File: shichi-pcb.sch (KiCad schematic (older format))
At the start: 27 parts, among them J1 USB_C_Receptacle_HRO_TYPE-C-3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, J2 Conn_01x04_Male, J3 Conn_01x06_Male, J4 Conn_01x04_Male, J5 Conn_01x01_Male, J6 Conn_01x01_Male, J7 Conn_01x01_Male, SW1 SW_Push, U1 USBLC6-2SC6, U2 ATmega32U4-AU, Y1 Crystal_GND24

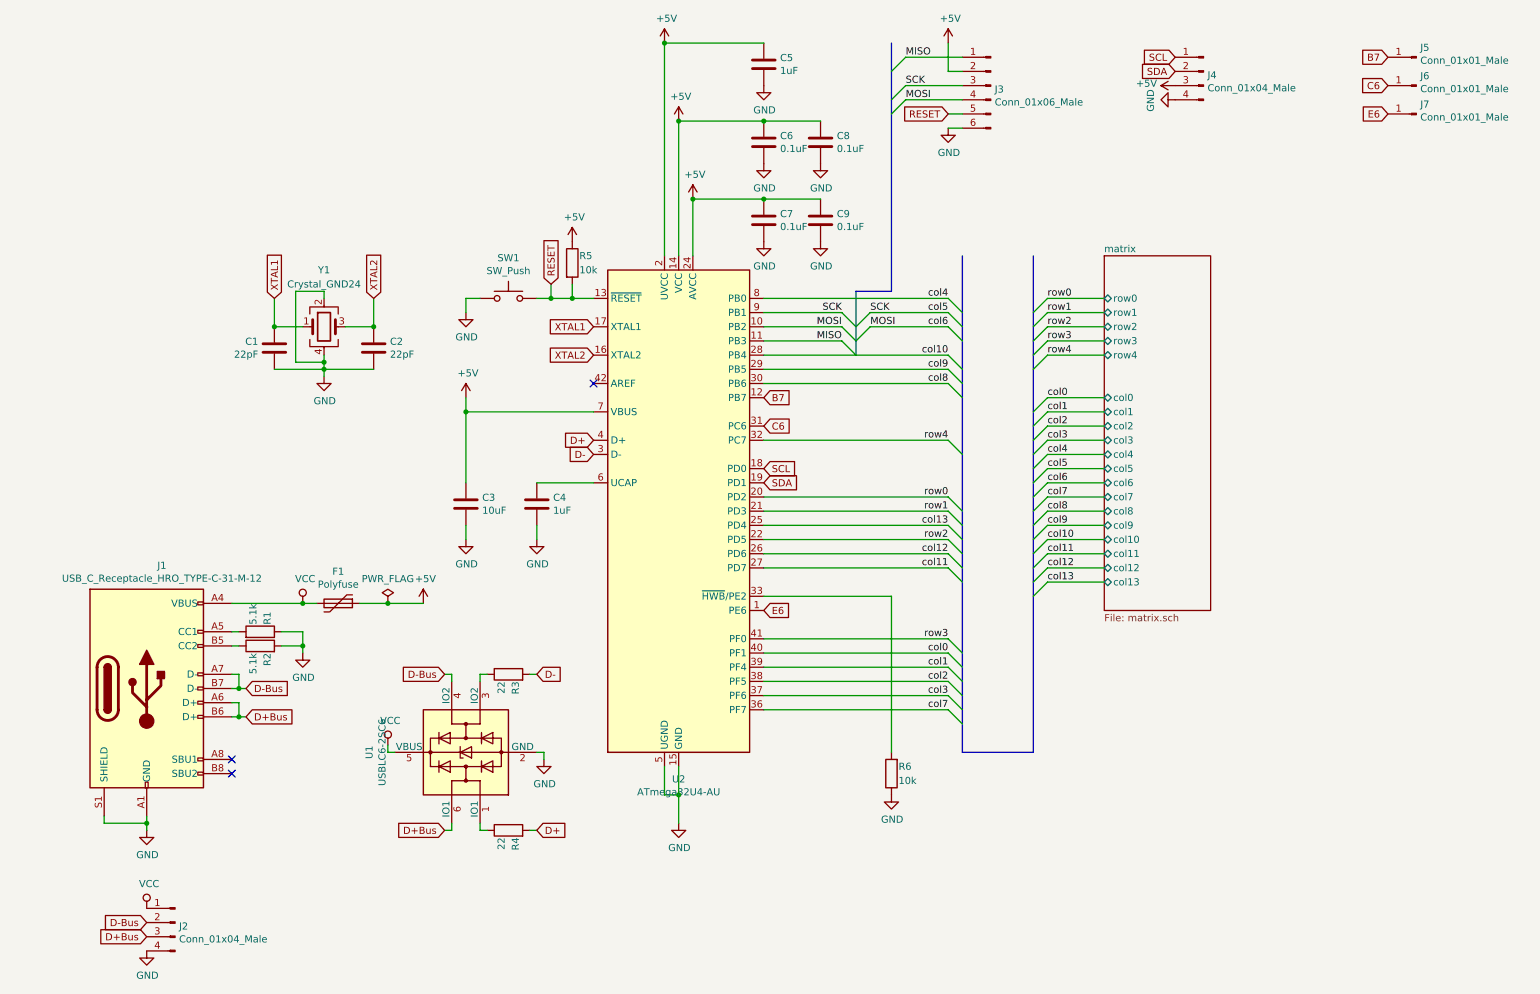
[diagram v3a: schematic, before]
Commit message: Initial port of STM32F072 arm processor
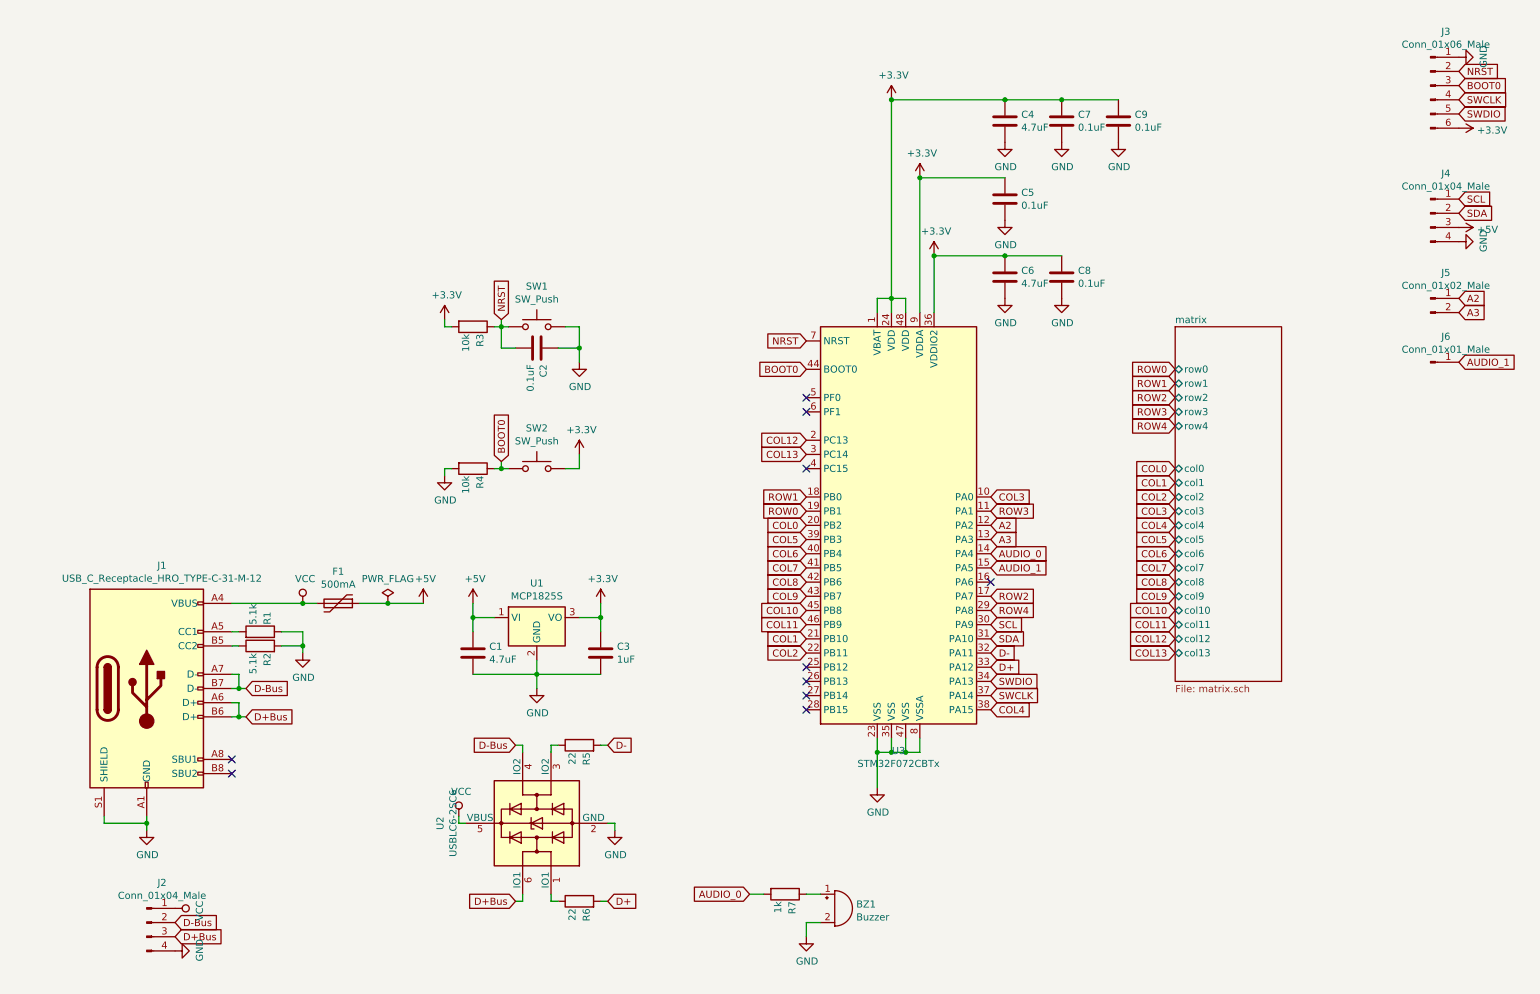
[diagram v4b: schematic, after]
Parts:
- removed C4: 1uF, Capacitor_SMD:C_0805_2012Metric_Pad1.15x1.40mm_HandSolder, symbol Device:C
- removed C8: 0.1uF, Capacitor_SMD:C_0805_2012Metric_Pad1.15x1.40mm_HandSolder, symbol Device:C
- removed J5, J7: Conn_01x01_Male, Connector_PinHeader_2.54mm:PinHeader_1x01_P2.54mm_Vertical, symbol Connector:Conn_01x01_Male
- removed R6: 10k, Resistor_SMD:R_0805_2012Metric_Pad1.15x1.40mm_HandSolder, symbol Device:R
- removed U2: ATmega32U4-AU, Package_QFP:TQFP-44_10x10mm_P0.8mm, symbol MCU_Microchip_ATmega:ATmega32U4-AU
- removed Y1: Crystal_GND24, Crystal:Crystal_SMD_SeikoEpson_FA238-4Pin_3.2x2.5mm_HandSoldering, symbol Device:Crystal_GND24
- added BZ1: Buzzer, symbol Device:Buzzer
- added C7, C9: 0.1uF, Capacitor_SMD:C_0805_2012Metric_Pad1.15x1.40mm_HandSolder, symbol Device:C
- added J5: Conn_01x02_Male, symbol Connector:Conn_01x02_Male
- added R4: 10k, Resistor_SMD:R_0805_2012Metric_Pad1.15x1.40mm_HandSolder, symbol Device:R
- added R7: 1k, Resistor_SMD:R_0805_2012Metric_Pad1.15x1.40mm_HandSolder, symbol Device:R
- added SW2: SW_Push, Button_Switch_SMD:SW_SPST_TL3342, symbol Switch:SW_Push
- added U1: MCP1825S, symbol Regulator_Linear:MCP1825S
- added U3: STM32F072CBTx, Package_QFP:LQFP-48_7x7mm_P0.5mm, symbol MCU_ST_STM32F0:STM32F072CBTx
- C1: value 22pF -> 4.7uF
- C2: value 22pF -> 0.1uF
- C3: value 10uF -> 1uF
- C4: renamed from C5; value 1uF -> 4.7uF
- C6: renamed from C7; value 0.1uF -> 4.7uF
- F1: value Polyfuse -> 500mA
- J2, J4: footprint Connector_PinHeader_2.54mm:PinHeader_1x04_P2.54mm_Vertical -> (none)
- J3: footprint Connector_PinHeader_2.54mm:PinHeader_1x06_P2.54mm_Vertical -> (none)
- J6: footprint Connector_PinHeader_2.54mm:PinHeader_1x01_P2.54mm_Vertical -> (none)
- renumbered C6 to C5, C9 to C8, R5 to R3, R3 to R5, R4 to R6, U1 to U2
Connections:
- net MISO is gone; now on net GND: J3.1 (Pin_1)
- net XTAL1 is gone; now on net GND: C1.2
- net XTAL2 is gone; now on net GND: C2.1
- net +5V: now also C1.1, U1.1 (VI); no longer C3.1, C4.1, C5.1, C6.1, C8.1, J3.2 (Pin_2), R3.1
- net D+: now also U3.33 (PA12)
- net D-: now also U3.32 (PA11)
- net GND: now also SW1.2, BZ1.2 (+), C7.2, C9.2, R4.2, U1.2 (GND), U3.23 (VSS), U3.35 (VSS), U3.47 (VSS), U3.8 (VSSA); no longer C1.1, C2.2, J3.6 (Pin_6), SW1.1
- net SCL: now also U3.30 (PA9)
- net SDA: now also U3.31 (PA10)
- net C6 renamed AUDIO_1
- net AUDIO_1: now also U3.15 (PA5)
- net MOSI renamed SWCLK
- net SWCLK: now also U3.37 (PA14)
- removed net RESET: J3.5 (Pin_5), R3.2, SW1.2
- net SCK renamed BOOT0
- net BOOT0: now also R4.1, SW2.1, U3.44 (BOOT0)
- new net: BZ1.1 (-), R7.1
- new net +3V3: C3.1, C4.1, C5.1, C6.1, C7.1, C8.1, C9.1, J3.6 (Pin_6), R3.2, SW2.2, U1.3 (VO), U3.1 (VBAT), U3.24 (VDD), U3.36 (VDDIO2), U3.48 (VDD), U3.9 (VDDA)
- new net A2: J5.1 (Pin_1), U3.12 (PA2)
- new net A3: J5.2 (Pin_2), U3.13 (PA3)
- new net AUDIO_0: R7.2, U3.14 (PA4)
- new net COL0: U3.20 (PB2)
- new net COL1: U3.21 (PB10)
- new net COL10: U3.45 (PB8)
- new net COL11: U3.46 (PB9)
- new net COL12: U3.2 (PC13)
- new net COL13: U3.3 (PC14)
- new net COL2: U3.22 (PB11)
- new net COL3: U3.10 (PA0)
- new net COL4: U3.38 (PA15)
- new net COL5: U3.39 (PB3)
- new net COL6: U3.40 (PB4)
- new net COL7: U3.41 (PB5)
- new net COL8: U3.42 (PB6)
- new net COL9: U3.43 (PB7)
- new net NRST: C2.2, J3.2 (Pin_2), R3.1, SW1.1, U3.7 (NRST)
- new net ROW0: U3.19 (PB1)
- new net ROW1: U3.18 (PB0)
- new net ROW2: U3.17 (PA7)
- new net ROW3: U3.11 (PA1)
- new net ROW4: U3.29 (PA8)
- new net SWDIO: J3.5 (Pin_5), U3.34 (PA13)
- no-connect marks 3 -> 10
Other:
- moved on the sheet: C4, C5, C6, C8, R3, R5, R6, SW1, U2

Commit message: Assign PCB Footprints to new additional schematics
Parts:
- BZ1: footprint (none) -> Buzzer_Beeper:Buzzer_Murata_PKMCS0909E4000-R1
- J2, J4: footprint (none) -> Connector_PinSocket_2.54mm:PinSocket_1x04_P2.54mm_Vertical
- J3: footprint (none) -> Connector_PinSocket_2.54mm:PinSocket_1x06_P2.54mm_Vertical
- J5: footprint (none) -> Connector_PinSocket_2.54mm:PinSocket_1x02_P2.54mm_Vertical
- J6: footprint (none) -> Connector_PinSocket_2.54mm:PinSocket_1x01_P2.54mm_Vertical
- U1: footprint (none) -> Package_TO_SOT_SMD:SOT-223
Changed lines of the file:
@@
 F 0 "U1" H 4000 5292 50  0000 C CNN
 F 1 "MCP1825S" H 4000 5201 50  0000 C CNN
-F 2 "" H 3900 5200 50  0001 C CNN
+F 2 "Package_TO_SOT_SMD:SOT-223" H 3900 5200 50  0001 C CNN
 F 3 "http://ww1.microchip.com/downloads/en/devicedoc/22056b.pdf" H 4000 5300 50  0001 C CNN
 	1    4000 5050
@@
 F 0 "J5" H 10408 2981 50  0000 C CNN
 F 1 "Conn_01x02_Male" H 10408 2890 50  0000 C CNN
-F 2 "" H 10300 2800 50  0001 C CNN
+F 2 "Connector_PinSocket_2.54mm:PinSocket_1x02_P2.54mm_Vertical" H 10300 2800 50  0001 C CNN
 F 3 "~" H 10300 2800 50  0001 C CNN
 	1    10300 2800
@@
 F 0 "J4" H 10408 2481 50  0000 C CNN
 F 1 "Conn_01x04_Male" H 10408 2390 50  0000 C CNN
-F 2 "" H 10300 2200 50  0001 C CNN
+F 2 "Connector_PinSocket_2.54mm:PinSocket_1x04_P2.54mm_Vertical" H 10300 2200 50  0001 C CNN
 F 3 "~" H 10300 2200 50  0001 C CNN
 	1    10300 2200
@@
 F 0 "J3" H 10408 1681 50  0000 C CNN
 F 1 "Conn_01x06_Male" H 10408 1590 50  0000 C CNN
-F 2 "" H 10300 1300 50  0001 C CNN
+F 2 "Connector_PinSocket_2.54mm:PinSocket_1x06_P2.54mm_Vertical" H 10300 1300 50  0001 C CNN
 F 3 "~" H 10300 1300 50  0001 C CNN
 	1    10300 1300
@@
 F 0 "J6" H 10408 3431 50  0000 C CNN
 F 1 "Conn_01x01_Male" H 10408 3340 50  0000 C CNN
-F 2 "" H 10300 3250 50  0001 C CNN
+F 2 "Connector_PinSocket_2.54mm:PinSocket_1x01_P2.54mm_Vertical" H 10300 3250 50  0001 C CNN
 F 3 "~" H 10300 3250 50  0001 C CNN
 	1    10300 3250
@@
 F 0 "BZ1" H 6252 7129 50  0000 L CNN
 F 1 "Buzzer" H 6252 7038 50  0000 L CNN
-F 2 "" V 6075 7200 50  0001 C CNN
+F 2 "Buzzer_Beeper:Buzzer_Murata_PKMCS0909E4000-R1" V 6075 7200 50  0001 C CNN
 F 3 "~" V 6075 7200 50  0001 C CNN
 	1    6100 7100
@@
 F 0 "J2" H 1358 7481 50  0000 C CNN
 F 1 "Conn_01x04_Male" H 1358 7390 50  0000 C CNN
-F 2 "" H 1250 7200 50  0001 C CNN
+F 2 "Connector_PinSocket_2.54mm:PinSocket_1x04_P2.54mm_Vertical" H 1250 7200 50  0001 C CNN
 F 3 "~" H 1250 7200 50  0001 C CNN
 	1    1250 7200

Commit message: Remove 22 ohm resistors from data lines
Stated in the STM32F072CB datasheet P.99:
No external termination series resistors are required on USB_DP (D+) and USB_DM (D-);
the matching impedance is already included in the embedded driver.
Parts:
- removed R5, R6: 22, Resistor_SMD:R_0805_2012Metric_Pad1.15x1.40mm_HandSolder, symbol Device:R
- renumbered R7 to R5
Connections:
- net D+: now also U2.1 (IO1)
- net D-: now also U2.3 (IO2)
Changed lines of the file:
@@
 	2350 5150 2350 5250
-Wire Wire Line
-	4450 7050 4500 7050
-Wire Wire Line
-	4450 5950 4500 5950
 Wire Wire Line
 	4550 6500 4550 6550
@@
 Wire Wire Line
 	4150 7050 4100 7050
-Text GLabel 4500 7050 2    50   Input ~ 0
+Text GLabel 4150 7050 2    50   Input ~ 0
 D+
 Wire Wire Line
@@
 Wire Wire Line
 	4150 5950 4100 5950
-Text GLabel 4500 5950 2    50   Input ~ 0
+Text GLabel 4150 5950 2    50   Input ~ 0
 D-
 Wire Wire Line
@@
 Text GLabel 3850 5950 0    50   Input ~ 0
 D-Bus
-$Comp
-L Device:R R6
-U 1 1 5CFC0556
-P 4300 7050
-F 0 "R6" H 4250 7000 50  0000 R CNN
-F 1 "22" H 4250 7100 50  0000 R CNN
-F 2 "Resistor_SMD:R_0805_2012Metric_Pad1.15x1.40mm_HandSolder" V 4230 7050 50  0001 C CNN
-F 3 "~" H 4300 7050 50  0001 C CNN
-	1    4300 7050
-	0    -1   -1   0
-$EndComp
-$Comp
-L Device:R R5
-U 1 1 5CFC2C41
-P 4300 5950
-F 0 "R5" H 4250 5900 50  0000 R CNN
-F 1 "22" H 4250 6000 50  0000 R CNN
-F 2 "Resistor_SMD:R_0805_2012Metric_Pad1.15x1.40mm_HandSolder" V 4230 5950 50  0001 C CNN
-F 3 "~" H 4300 5950 50  0001 C CNN
-	1    4300 5950
-	0    -1   -1   0
-$EndComp
 $Comp
 L Power_Protection:USBLC6-2SC6 U2
@@
 AUDIO_0
 $Comp
-L Device:R R7
+L Device:R R5
 U 1 1 5D35C35E
 P 5750 7000
-F 0 "R7" H 5800 7050 50  0000 L CNN
+F 0 "R5" H 5800 7050 50  0000 L CNN
 F 1 "1k" H 5800 6950 50  0000 L CNN
 F 2 "Resistor_SMD:R_0805_2012Metric_Pad1.15x1.40mm_HandSolder" V 5680 7000 50  0001 C CNN

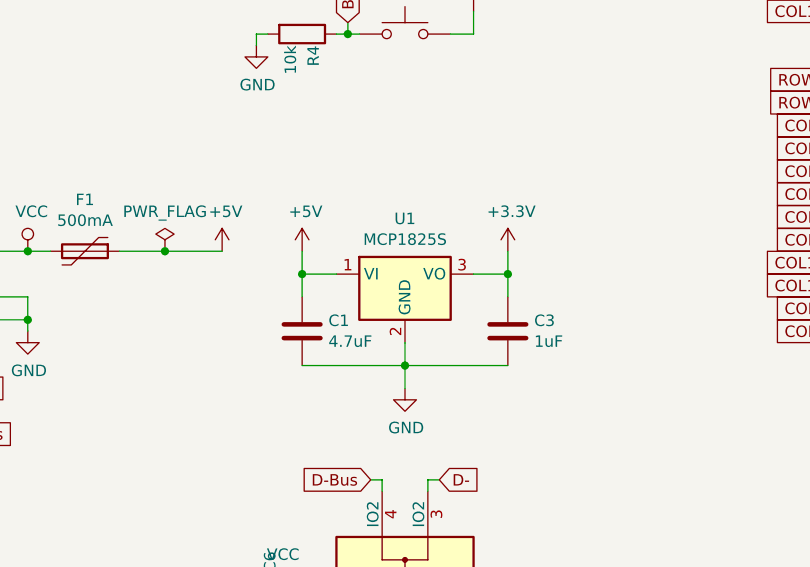
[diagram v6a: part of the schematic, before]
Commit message: Replace MCP1825S with MCP1700-3302E LDO voltage regulator
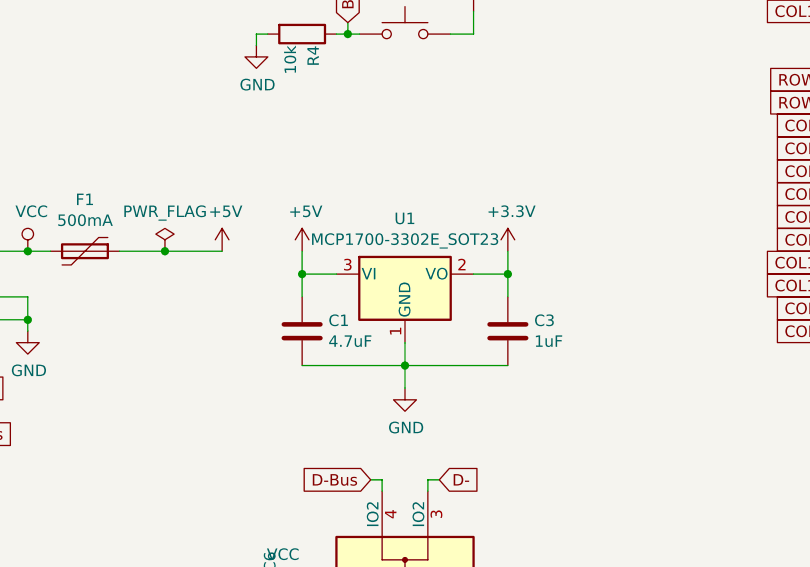
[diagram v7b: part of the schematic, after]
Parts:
- removed U1: MCP1825S, Package_TO_SOT_SMD:SOT-223, symbol Regulator_Linear:MCP1825S
- added U1: MCP1700-3302E_SOT23, Package_TO_SOT_SMD:SOT-23, symbol Regulator_Linear:MCP1700-3302E_SOT23
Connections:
- net +3V3: now also U1.2 (VO)
- net +5V: now also U1.3 (VI)
- net GND: now also U1.1 (GND)
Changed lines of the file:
@@
-$EndComp
-$Comp
-L Regulator_Linear:MCP1825S U1
-U 1 1 5D192517
-P 4000 5050
-F 0 "U1" H 4000 5292 50  0000 C CNN
-F 1 "MCP1825S" H 4000 5201 50  0000 C CNN
-F 2 "Package_TO_SOT_SMD:SOT-223" H 3900 5200 50  0001 C CNN
-F 3 "http://ww1.microchip.com/downloads/en/devicedoc/22056b.pdf" H 4000 5300 50  0001 C CNN
-	1    4000 5050
-	1    0    0    -1
 $EndComp
 $Comp
@@
 Text GLabel 1450 7200 2    50   Input ~ 0
 D-Bus
+$Comp
+L Regulator_Linear:MCP1700-3302E_SOT23 U1
+U 1 1 5D1F289F
+P 4000 5050
+F 0 "U1" H 4000 5292 50  0000 C CNN
+F 1 "MCP1700-3302E_SOT23" H 4000 5201 50  0000 C CNN
+F 2 "Package_TO_SOT_SMD:SOT-23" H 4000 5275 50  0001 C CNN
+F 3 "http://ww1.microchip.com/downloads/en/DeviceDoc/20001826D.pdf" H 4000 5050 50  0001 C CNN
+	1    4000 5050
+	1    0    0    -1
+$EndComp
 $EndSCHEMATC
